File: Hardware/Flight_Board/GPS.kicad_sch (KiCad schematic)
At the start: 1 part, among them U6 CAM-M8Q-0

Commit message: Make GPS
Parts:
- added C17: 4.7u, symbol Device:C
- added R1, R2: 220, symbol Device:R
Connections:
- net +3.3V: now reaches U6.1 (VCC_IO)
- net +3.3V: now also U6.8 (V_BCKP), U6.9 (VCC), C17.1
- net GND: now reaches U6.10 (GND)
- net GND: now also U6.11 (GND), U6.12 (GND), U6.13 (GND), U6.14 (GND), U6.15 (GND), U6.18 (GND), U6.19 (GND), U6.21 (GND), U6.22 (GND), U6.27 (GND), U6.31 (GND), U6.4 (GND), U6.5 (GND), C17.2
- net at U6.16 (RF_OUT): now also U6.17 (RF_IN)
- net DSEL: now reaches U6.20 (DSEL)
- net at U6.25 (TXD/SPI_MISO): now also R1.1
- net at U6.26 (RXD/SPI_MOSI): now also R2.2
- net SDA: now reaches U6.3 (SDA/SPI_CS_N)
- net SCL: now reaches U6.6 (SCL/SPI_CLK)
- net EXTINT: now reaches U6.7 (EXTINT)
- new net RXD: R2.1
- new net TXD: R1.2
- no-connect marks 0 -> 6

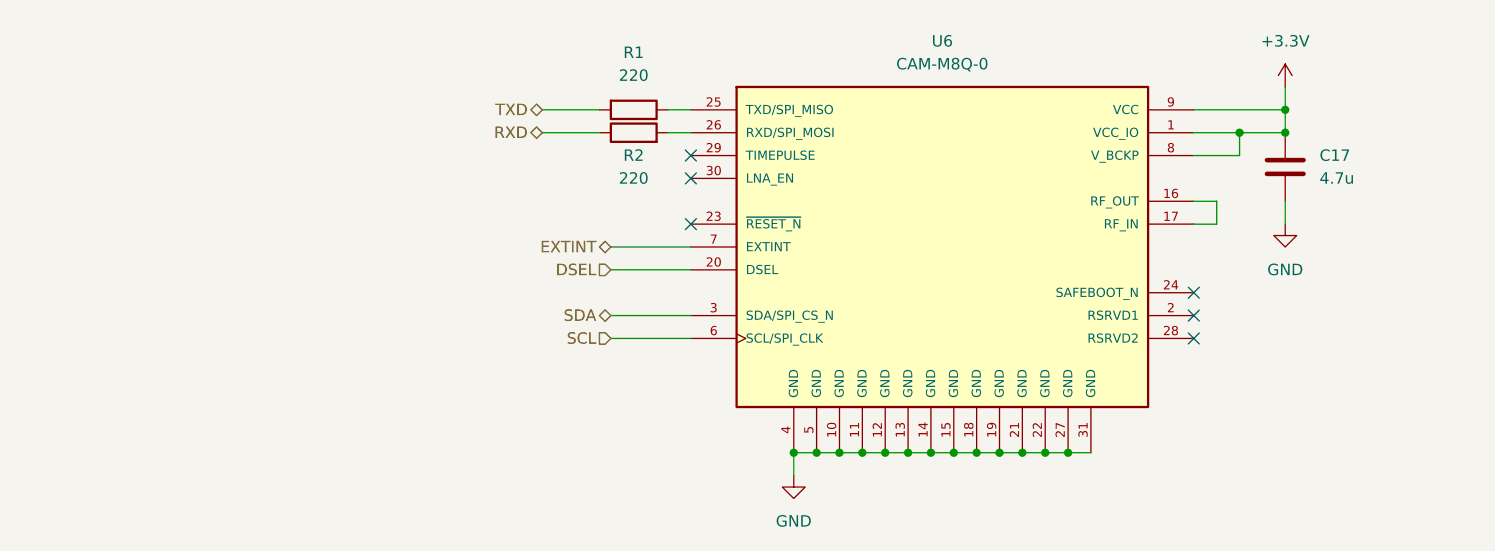
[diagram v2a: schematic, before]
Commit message: move ADLX375 to I2C, bring out more mcu pins, and general touchups
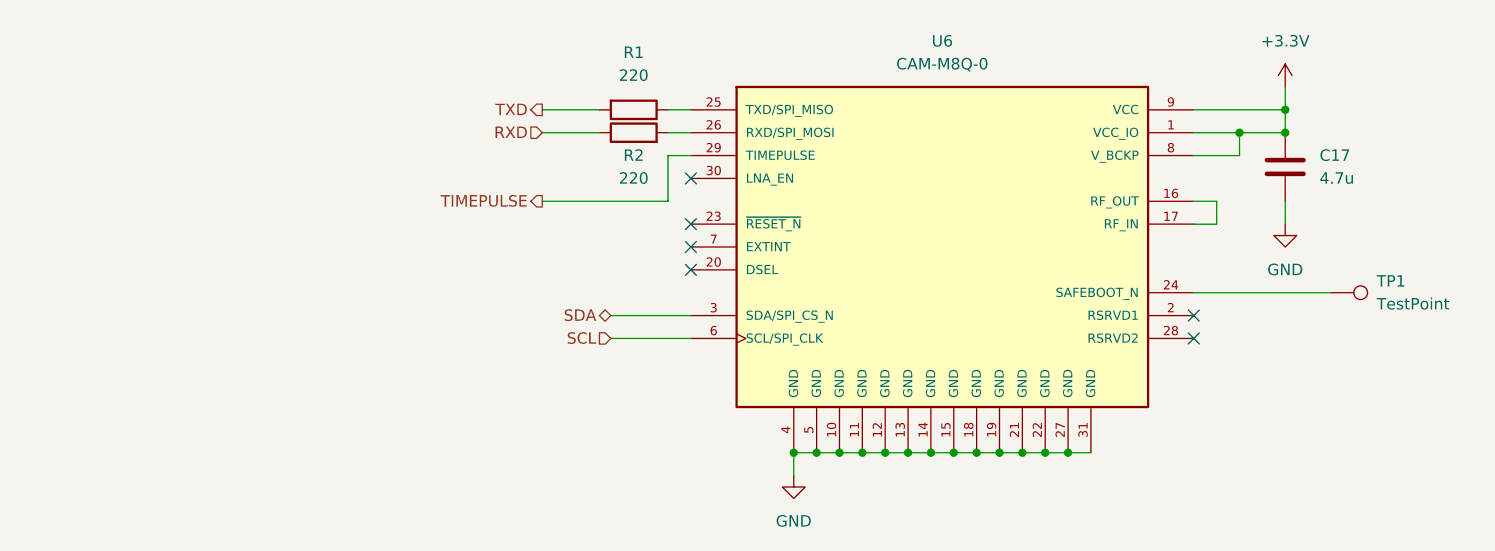
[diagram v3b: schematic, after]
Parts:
- added TP1: TestPoint, symbol Connector:TestPoint
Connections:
- net at U6.24 (SAFEBOOT_N): now also TP1.1
- net TIMEPULSE: now reaches U6.29 (TIMEPULSE)
- net DSEL: no longer names the net of U6.20 (DSEL)
- net EXTINT: no longer names the net of U6.7 (EXTINT)
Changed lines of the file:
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@@
   (junction (at 177.8 100.33) (diameter 0) (color 0 0 0 0)
   )
-  (no_connect (at 201.93 82.55))
+  (no_connect (at 146.05 77.47))
   (no_connect (at 146.05 69.85))
   (no_connect (at 201.93 85.09))
   (no_connect (at 146.05 74.93))
   (no_connect (at 201.93 87.63))
-  (no_connect (at 146.05 67.31))
+  (no_connect (at 146.05 80.01))
   (wire (pts (xy 137.16 85.09) (xy 146.05 85.09))
     (stroke (width 0) (type default))
@@
     (stroke (width 0) (type default))
   )
-  (wire (pts (xy 146.05 77.47) (xy 137.16 77.47))
-    (stroke (width 0) (type default))
-  )
   (wire (pts (xy 180.34 100.33) (xy 182.88 100.33))
     (stroke (width 0) (type default))
@@
     (stroke (width 0) (type default))
   )
+  (wire (pts (xy 129.54 72.39) (xy 143.51 72.39))
+    (stroke (width 0) (type default))
+  )
   (wire (pts (xy 172.72 100.33) (xy 175.26 100.33))
     (stroke (width 0) (type default))
@@
     (stroke (width 0) (type default))
   )
+  (wire (pts (xy 201.93 82.55) (xy 217.17 82.55))
+    (stroke (width 0) (type default))
+  )
   (wire (pts (xy 182.88 100.33) (xy 185.42 100.33))
     (stroke (width 0) (type default))
@@
     (stroke (width 0) (type default))
   )
-  (wire (pts (xy 137.16 80.01) (xy 146.05 80.01))
-    (stroke (width 0) (type default))
-  )
   (wire (pts (xy 143.51 64.77) (xy 146.05 64.77))
     (stroke (width 0) (type default))
@@
     (stroke (width 0) (type default))
   )
+  (wire (pts (xy 143.51 67.31) (xy 143.51 72.39))
+    (stroke (width 0) (type default))
+  )
   (wire (pts (xy 162.56 100.33) (xy 165.1 100.33))
     (stroke (width 0) (type default))
   )
+  (wire (pts (xy 146.05 67.31) (xy 143.51 67.31))
+    (stroke (width 0) (type default))
+  )
   (wire (pts (xy 165.1 100.33) (xy 167.64 100.33))
     (stroke (width 0) (type default))
@@
     (effects (font (size 1.27 1.27)) (justify right))
   )
-  (hierarchical_label "EXTINT" (shape bidirectional) (at 137.16 77.47 180) (fields_autoplaced)
-    (effects (font (size 1.27 1.27)) (justify right))
-  )
-  (hierarchical_label "RXD" (shape bidirectional) (at 129.54 64.77 180) (fields_autoplaced)
-    (effects (font (size 1.27 1.27)) (justify right))
-  )
-  (hierarchical_label "DSEL" (shape input) (at 137.16 80.01 180) (fields_autoplaced)
-    (effects (font (size 1.27 1.27)) (justify right))
-  )
-  (hierarchical_label "TXD" (shape bidirectional) (at 129.54 62.23 180) (fields_autoplaced)
+  (hierarchical_label "RXD" (shape input) (at 129.54 64.77 180) (fields_autoplaced)
+    (effects (font (size 1.27 1.27)) (justify right))
+  )
+  (hierarchical_label "TIMEPULSE" (shape output) (at 129.54 72.39 180) (fields_autoplaced)
+    (effects (font (size 1.27 1.27)) (justify right))
+  )
+  (hierarchical_label "TXD" (shape output) (at 129.54 62.23 180) (fields_autoplaced)
     (effects (font (size 1.27 1.27)) (justify right))
   )
@@
         )
       )
+    )
+  )
+  (symbol (lib_id "Connector:TestPoint") (at 217.17 82.55 270) (unit 1)
+    (in_bom yes) (on_board yes) (dnp no) (fields_autoplaced)
+    (property "Reference" "TP1" (at 222.25 81.28 90)
+      (effects (font (size 1.27 1.27)) (justify left))
+    )
+    (property "Value" "TestPoint" (at 222.25 83.82 90)
+      (effects (font (size 1.27 1.27)) (justify left))
+    )
+    (property "Footprint" "" (at 217.17 87.63 0)
+      (effects (font (size 1.27 1.27)) hide)
+    )
+    (property "Datasheet" "~" (at 217.17 87.63 0)
+      (effects (font (size 1.27 1.27)) hide)
+    )
+    (pin "1")
+    (instances
+      (project "Flight_Board"
+        (path "/e8eb85d5-f1ff-4500-895d-25b9ff5f6d36/52cae81a-54fe-42c0-9a19-be88b271d004"
+          (reference "TP1") (unit 1)
+        )
+      )

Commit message: clean up and finalize initial design
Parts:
- renumbered R1 to R4, R2 to R5, U6 to U5
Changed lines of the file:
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@@
   (symbol (lib_id "Device:R") (at 139.7 62.23 270) (unit 1)
     (in_bom yes) (on_board yes) (dnp no) (fields_autoplaced)
-    (property "Reference" "R1" (at 139.7 55.88 90)
+    (property "Reference" "R4" (at 139.7 55.88 90)
       (effects (font (size 1.27 1.27)))
     )
@@
       (project "Flight_Board"
         (path "/e8eb85d5-f1ff-4500-895d-25b9ff5f6d36/52cae81a-54fe-42c0-9a19-be88b271d004"
-          (reference "R1") (unit 1)
+          (reference "R4") (unit 1)
         )
       )
@@
   (symbol (lib_id "power:GND") (at 212.09 74.93 0) (unit 1)
     (in_bom yes) (on_board yes) (dnp no) (fields_autoplaced)
-    (property "Reference" "#PWR032" (at 212.09 81.28 0)
+    (property "Reference" "#PWR033" (at 212.09 81.28 0)
       (effects (font (size 1.27 1.27)) hide)
     )
@@
       (project "Flight_Board"
         (path "/e8eb85d5-f1ff-4500-895d-25b9ff5f6d36/52cae81a-54fe-42c0-9a19-be88b271d004"
-          (reference "#PWR032") (unit 1)
+          (reference "#PWR033") (unit 1)
         )
       )
@@
   (symbol (lib_id "Project:CAM-M8Q-0") (at 173.99 77.47 0) (unit 1)
     (in_bom yes) (on_board yes) (dnp no) (fields_autoplaced)
-    (property "Reference" "U6" (at 173.99 54.61 0)
+    (property "Reference" "U5" (at 173.99 54.61 0)
       (effects (font (size 1.27 1.27)))
     )
@@
       (project "Flight_Board"
         (path "/e8eb85d5-f1ff-4500-895d-25b9ff5f6d36/52cae81a-54fe-42c0-9a19-be88b271d004"
-          (reference "U6") (unit 1)
+          (reference "U5") (unit 1)
         )
       )
@@
   (symbol (lib_id "Device:R") (at 139.7 64.77 90) (unit 1)
     (in_bom yes) (on_board yes) (dnp no)
-    (property "Reference" "R2" (at 139.7 67.31 90)
+    (property "Reference" "R5" (at 139.7 67.31 90)
       (effects (font (size 1.27 1.27)))
     )
@@
       (project "Flight_Board"
         (path "/e8eb85d5-f1ff-4500-895d-25b9ff5f6d36/52cae81a-54fe-42c0-9a19-be88b271d004"
-          (reference "R2") (unit 1)
+          (reference "R5") (unit 1)
         )
       )
@@
   (symbol (lib_id "power:+3.3V") (at 212.09 59.69 0) (unit 1)
     (in_bom yes) (on_board yes) (dnp no) (fields_autoplaced)
-    (property "Reference" "#PWR033" (at 212.09 63.5 0)
+    (property "Reference" "#PWR032" (at 212.09 63.5 0)
       (effects (font (size 1.27 1.27)) hide)
     )
@@
       (project "Flight_Board"
         (path "/e8eb85d5-f1ff-4500-895d-25b9ff5f6d36/52cae81a-54fe-42c0-9a19-be88b271d004"
-          (reference "#PWR033") (unit 1)
+          (reference "#PWR032") (unit 1)
         )
       )

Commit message: Clean up, relabel all refdes, and add autosaved files to gitignore
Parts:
- renumbered R4 to R6, R5 to R7
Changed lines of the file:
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@@
   (symbol (lib_id "Device:R") (at 139.7 62.23 270) (unit 1)
     (in_bom yes) (on_board yes) (dnp no) (fields_autoplaced)
-    (property "Reference" "R4" (at 139.7 55.88 90)
+    (property "Reference" "R6" (at 139.7 55.88 90)
       (effects (font (size 1.27 1.27)))
     )
@@
       (project "Flight_Board"
         (path "/e8eb85d5-f1ff-4500-895d-25b9ff5f6d36/52cae81a-54fe-42c0-9a19-be88b271d004"
-          (reference "R4") (unit 1)
+          (reference "R6") (unit 1)
         )
       )
@@
   (symbol (lib_id "power:GND") (at 212.09 74.93 0) (unit 1)
     (in_bom yes) (on_board yes) (dnp no) (fields_autoplaced)
-    (property "Reference" "#PWR033" (at 212.09 81.28 0)
+    (property "Reference" "#PWR034" (at 212.09 81.28 0)
       (effects (font (size 1.27 1.27)) hide)
     )
@@
       (project "Flight_Board"
         (path "/e8eb85d5-f1ff-4500-895d-25b9ff5f6d36/52cae81a-54fe-42c0-9a19-be88b271d004"
-          (reference "#PWR033") (unit 1)
+          (reference "#PWR034") (unit 1)
         )
       )
@@
   (symbol (lib_id "Device:R") (at 139.7 64.77 90) (unit 1)
     (in_bom yes) (on_board yes) (dnp no)
-    (property "Reference" "R5" (at 139.7 67.31 90)
+    (property "Reference" "R7" (at 139.7 67.31 90)
       (effects (font (size 1.27 1.27)))
     )
@@
       (project "Flight_Board"
         (path "/e8eb85d5-f1ff-4500-895d-25b9ff5f6d36/52cae81a-54fe-42c0-9a19-be88b271d004"
-          (reference "R5") (unit 1)
+          (reference "R7") (unit 1)
         )
       )
@@
   (symbol (lib_id "power:+3.3V") (at 212.09 59.69 0) (unit 1)
     (in_bom yes) (on_board yes) (dnp no) (fields_autoplaced)
-    (property "Reference" "#PWR032" (at 212.09 63.5 0)
+    (property "Reference" "#PWR033" (at 212.09 63.5 0)
       (effects (font (size 1.27 1.27)) hide)
     )
@@
       (project "Flight_Board"
         (path "/e8eb85d5-f1ff-4500-895d-25b9ff5f6d36/52cae81a-54fe-42c0-9a19-be88b271d004"
+          (reference "#PWR033") (unit 1)
+        )
+      )
+    )
+  )
+  (symbol (lib_id "power:GND") (at 157.48 102.87 0) (unit 1)
+    (in_bom yes) (on_board yes) (dnp no) (fields_autoplaced)
+    (property "Reference" "#PWR032" (at 157.48 109.22 0)
+      (effects (font (size 1.27 1.27)) hide)
+    )
+    (property "Value" "GND" (at 157.48 107.95 0)
+      (effects (font (size 1.27 1.27)))
+    )
+    (property "Footprint" "" (at 157.48 102.87 0)
+      (effects (font (size 1.27 1.27)) hide)
+    )
+    (property "Datasheet" "" (at 157.48 102.87 0)
+      (effects (font (size 1.27 1.27)) hide)
+    )
+    (pin "1")
+    (instances
+      (project "Flight_Board"
+        (path "/e8eb85d5-f1ff-4500-895d-25b9ff5f6d36/52cae81a-54fe-42c0-9a19-be88b271d004"
           (reference "#PWR032") (unit 1)
         )
       )
-    )
-  )
-  (symbol (lib_id "power:GND") (at 157.48 102.87 0) (unit 1)
-    (in_bom yes) (on_board yes) (dnp no) (fields_autoplaced)
-    (property "Reference" "#PWR031" (at 157.48 109.22 0)
-      (effects (font (size 1.27 1.27)) hide)
-    )
-    (property "Value" "GND" (at 157.48 107.95 0)
-      (effects (font (size 1.27 1.27)))
-    )
-    (property "Footprint" "" (at 157.48 102.87 0)
-      (effects (font (size 1.27 1.27)) hide)
-    )
-    (property "Datasheet" "" (at 157.48 102.87 0)
-      (effects (font (size 1.27 1.27)) hide)
-    )
-    (pin "1")
-    (instances
-      (project "Flight_Board"
-        (path "/e8eb85d5-f1ff-4500-895d-25b9ff5f6d36/52cae81a-54fe-42c0-9a19-be88b271d004"
-          (reference "#PWR031") (unit 1)
-        )
-      )

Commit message: clean up, implement suggestions from saunders
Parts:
- added D1: LED, symbol Device:LED
- added R26: 1k, symbol Device:R
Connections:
- net +3.3V: now also D1.2 (A)
- net SCL: no longer names the net of U5.6 (SCL/SPI_CLK)
- net SDA: no longer names the net of U5.3 (SDA/SPI_CS_N)
- net TIMEPULSE: no longer names the net of U5.29 (TIMEPULSE)
- net TIMEPULSE: now also R26.2
- new net: D1.1 (K), R26.1
- no-connect marks 6 -> 8
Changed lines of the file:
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@@
   (no_connect (at 146.05 69.85))
   (no_connect (at 201.93 85.09))
+  (no_connect (at 146.05 85.09))
   (no_connect (at 146.05 74.93))
   (no_connect (at 201.93 87.63))
+  (no_connect (at 146.05 87.63))
   (no_connect (at 146.05 80.01))
-  (wire (pts (xy 137.16 85.09) (xy 146.05 85.09))
-    (stroke (width 0) (type default))
-  )
   (wire (pts (xy 212.09 62.23) (xy 212.09 64.77))
     (stroke (width 0) (type default))
   )
-  (wire (pts (xy 137.16 87.63) (xy 146.05 87.63))
-    (stroke (width 0) (type default))
-  )
   (wire (pts (xy 177.8 100.33) (xy 180.34 100.33))
     (stroke (width 0) (type default))
@@
     (stroke (width 0) (type default))
   )
+  (wire (pts (xy 114.3 72.39) (xy 109.22 72.39))
+    (stroke (width 0) (type default))
+  )
   (wire (pts (xy 204.47 74.93) (xy 204.47 72.39))
     (stroke (width 0) (type default))
@@
     (stroke (width 0) (type default))
   )
+  (wire (pts (xy 109.22 69.85) (xy 109.22 72.39))
+    (stroke (width 0) (type default))
+  )
   (wire (pts (xy 201.93 82.55) (xy 217.17 82.55))
     (stroke (width 0) (type default))
@@
   (wire (pts (xy 201.93 62.23) (xy 212.09 62.23))
     (stroke (width 0) (type default))
-  )
-  (hierarchical_label "SCL" (shape input) (at 137.16 87.63 180) (fields_autoplaced)
-    (effects (font (size 1.27 1.27)) (justify right))
-  )
-  (hierarchical_label "SDA" (shape bidirectional) (at 137.16 85.09 180) (fields_autoplaced)
-    (effects (font (size 1.27 1.27)) (justify right))
   )
   (hierarchical_label "RXD" (shape input) (at 129.54 64.77 180) (fields_autoplaced)
     (effects (font (size 1.27 1.27)) (justify right))
   )
-  (hierarchical_label "TIMEPULSE" (shape output) (at 129.54 72.39 180) (fields_autoplaced)
-    (effects (font (size 1.27 1.27)) (justify right))
-  )
   (hierarchical_label "TXD" (shape output) (at 129.54 62.23 180) (fields_autoplaced)
     (effects (font (size 1.27 1.27)) (justify right))
+  )
+  (symbol (lib_id "Device:LED") (at 118.11 72.39 180) (unit 1)
+    (in_bom yes) (on_board yes) (dnp no) (fields_autoplaced)
+    (property "Reference" "D1" (at 119.6975 64.77 0)
+      (effects (font (size 1.27 1.27)))
+    )
+    (property "Value" "LED" (at 119.6975 67.31 0)
+      (effects (font (size 1.27 1.27)))
+    )
+    (property "Footprint" "" (at 118.11 72.39 0)
+      (effects (font (size 1.27 1.27)) hide)
+    )
+    (property "Datasheet" "~" (at 118.11 72.39 0)
+      (effects (font (size 1.27 1.27)) hide)
+    )
+    (pin "1")
+    (pin "2")
+    (instances
+      (project "Flight_Board"
+        (path "/e8eb85d5-f1ff-4500-895d-25b9ff5f6d36/52cae81a-54fe-42c0-9a19-be88b271d004"
+          (reference "D1") (unit 1)
+        )
+      )
+    )
   )
   (symbol (lib_id "Device:R") (at 139.7 62.23 270) (unit 1)
@@
         )
       )
+    )
+  )
+  (symbol (lib_id "Device:R") (at 125.73 72.39 90) (unit 1)
+    (in_bom yes) (on_board yes) (dnp no)
+    (property "Reference" "R26" (at 125.73 74.93 90)
+      (effects (font (size 1.27 1.27)))
+    )
+    (property "Value" "1k" (at 125.73 77.47 90)
+      (effects (font (size 1.27 1.27)))
+    )
+    (property "Footprint" "" (at 125.73 74.168 90)
+      (effects (font (size 1.27 1.27)) hide)
+    )
+    (property "Datasheet" "~" (at 125.73 72.39 0)
+      (effects (font (size 1.27 1.27)) hide)
+    )
+    (pin "1")
+    (pin "2")
+    (instances
+      (project "Flight_Board"
+        (path "/e8eb85d5-f1ff-4500-895d-25b9ff5f6d36/52cae81a-54fe-42c0-9a19-be88b271d004"
+          (reference "R26") (unit 1)
+        )
+      )
+    )
+  )
+  (symbol (lib_id "power:+3.3V") (at 109.22 69.85 0) (unit 1)
+    (in_bom yes) (on_board yes) (dnp no) (fields_autoplaced)
+    (property "Reference" "#PWR063" (at 109.22 73.66 0)
+      (effects (font (size 1.27 1.27)) hide)
+    )
+    (property "Value" "+3.3V" (at 109.22 64.77 0)
+      (effects (font (size 1.27 1.27)))
+    )
+    (property "Footprint" "" (at 109.22 69.85 0)
+      (effects (font (size 1.27 1.27)) hide)
+    )
+    (property "Datasheet" "" (at 109.22 69.85 0)
+      (effects (font (size 1.27 1.27)) hide)
+    )
+    (pin "1")
+    (instances
+      (project "Flight_Board"
+        (path "/e8eb85d5-f1ff-4500-895d-25b9ff5f6d36/52cae81a-54fe-42c0-9a19-be88b271d004"
+          (reference "#PWR063") (unit 1)
+        )
+      )
